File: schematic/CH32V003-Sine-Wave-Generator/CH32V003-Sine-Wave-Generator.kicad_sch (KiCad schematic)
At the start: 5 parts, among them U1 CH32V003JxMx, Y1 24MHz

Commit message: Update schematics
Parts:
- U1: value CH32V003JxMx -> CH32V003J4M6
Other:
- moved on the sheet: C1, C2, R1, U1, Y1

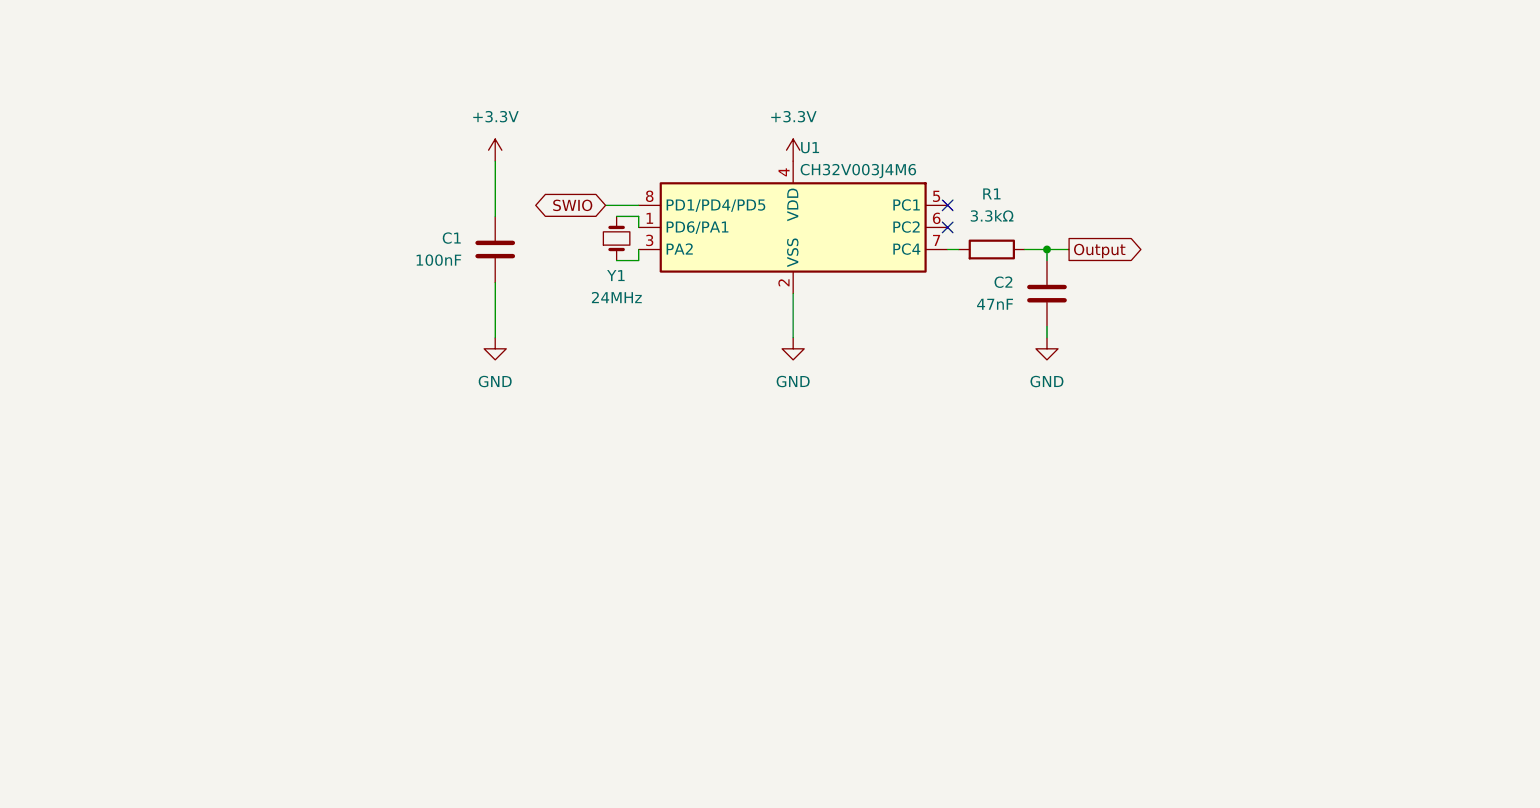
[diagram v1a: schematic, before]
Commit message: Add OPAMP to convert unipolar wave to bipolar wave
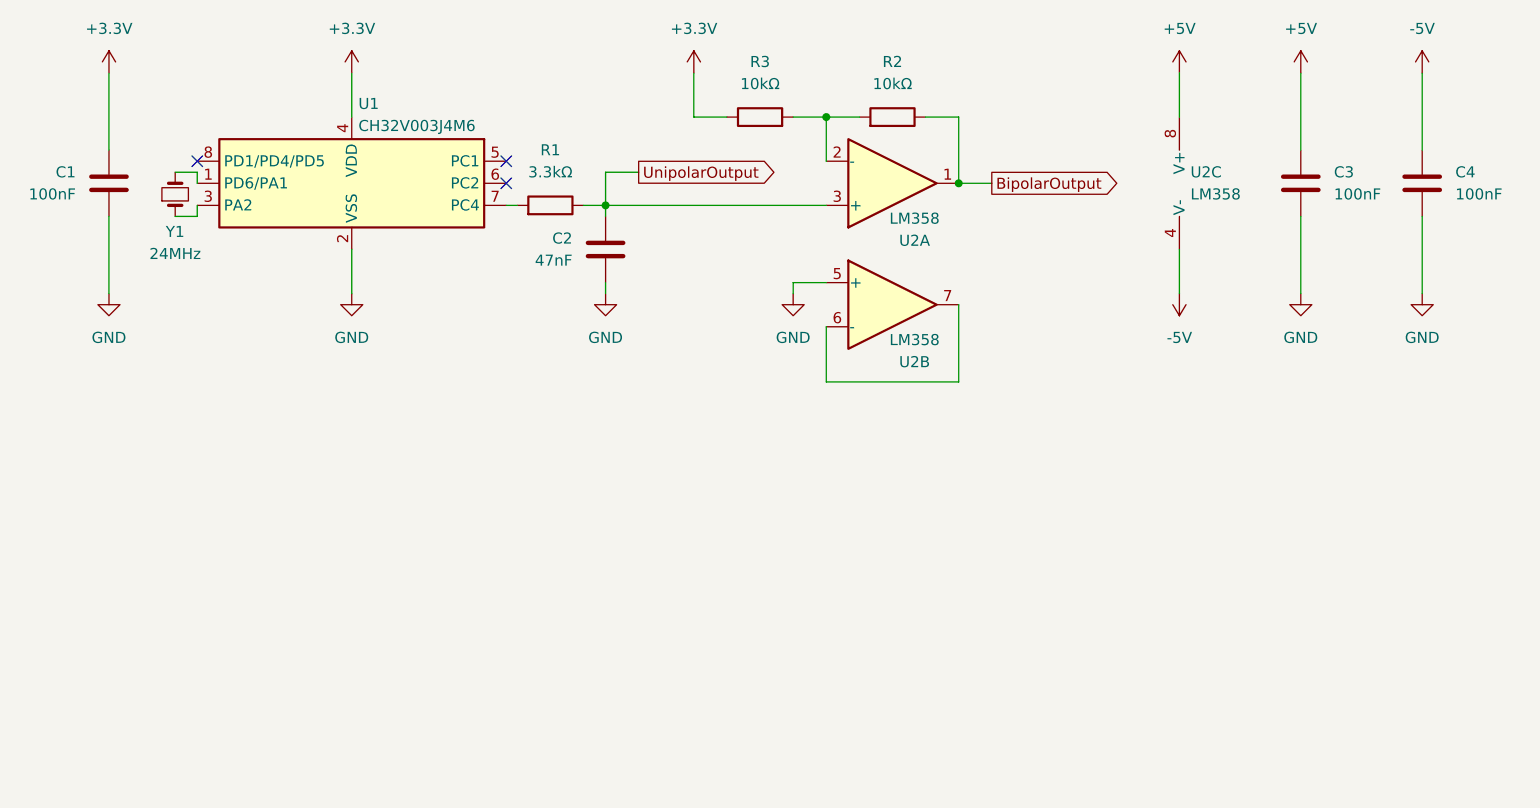
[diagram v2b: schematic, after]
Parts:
- added C3, C4: 100nF, symbol Device:C
- added R2, R3: 10kΩ, symbol Device:R
- added U2: LM358, symbol Amplifier_Operational:LM358
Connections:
- net +3.3V: now also R3.1
- net GND: now also C3.2, C4.2, U2.5 (+)
- net Output renamed UnipolarOutput
- net UnipolarOutput: now also U2.3 (+)
- net SWIO: no longer names the net of U1.8 (PD1/PD4/PD5)
- new net: R2.2, R3.2, U2.2 (-)
- new net: U2.6 (-), U2.7
- new net +5V: C3.1, U2.8 (V+)
- new net -5V: C4.1, U2.4 (V-)
- new net BipolarOutput: R2.1, U2.1
- no-connect marks 2 -> 3
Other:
- moved on the sheet: C1, C2, R1, U1, Y1
